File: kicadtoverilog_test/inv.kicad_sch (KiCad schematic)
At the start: 1 part, among them U4 NOT

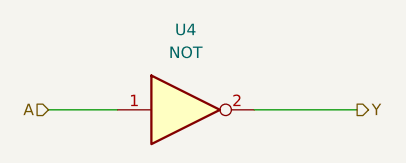
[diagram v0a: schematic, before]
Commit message: Seems to generate the proper per-page netlist now!
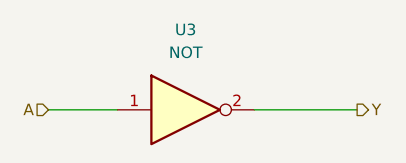
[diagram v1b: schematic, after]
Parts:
- renumbered U4 to U3
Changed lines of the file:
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@@
   (symbol (lib_id "VerilogLibrary:NOT") (at 78.74 44.45 0)
     (in_bom yes) (on_board yes) (fields_autoplaced)
-    (property "Reference" "U4" (id 0) (at 78.74 35.56 0))
+    (property "Reference" "U3" (id 0) (at 78.74 35.56 0))
     (property "Value" "NOT" (id 1) (at 78.74 38.1 0))
     (property "Footprint" "" (id 2) (at 78.74 44.45 0)

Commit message: Update symbol pins to use pin names and not pin numbers, to match sheets
Update module/sheet names to drop the '_kicad_sch' suffix
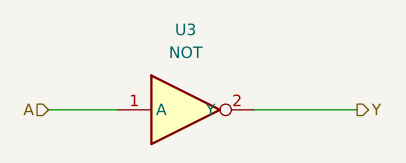
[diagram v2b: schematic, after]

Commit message: Switch to KiCad 6.0 release
Use Command line args with argparse
Add some docs
Copy over synthesis_defs.v to verilog directory during run
Regularize logging
Fix bug with single nets on two module pins (Use wire statements for all nets, with assign statements for each module pin.)
Add test block with big divby3 from Atari TIA chip
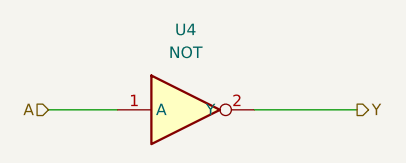
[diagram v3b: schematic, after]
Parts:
- renumbered U3 to U4
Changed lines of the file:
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@@
 (kicad_sch (version 20211123) (generator eeschema)
-  (paper "A4")
+  (paper "USLetter")
   (wire (pts (xy 86.36 44.45) (xy 97.79 44.45))
     (stroke (width 0) (type default) (color 0 0 0 0))
@@
   (symbol (lib_id "VerilogLibrary:NOT") (at 78.74 44.45 0)
     (in_bom yes) (on_board yes) (fields_autoplaced)
-    (property "Reference" "U3" (id 0) (at 78.74 35.56 0))
+    (property "Reference" "U4" (id 0) (at 78.74 35.56 0))
     (property "Value" "NOT" (id 1) (at 78.74 38.1 0))
     (property "Footprint" "" (id 2) (at 78.74 44.45 0)
